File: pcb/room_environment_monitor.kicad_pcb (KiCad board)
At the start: 2 copper layers, 1 part, among them U2 ESP32-C3-MINI-1

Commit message: get the schematic done, need to optomize for parts
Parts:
- added U1: D1213A-04V, Package_TO_SOT_SMD:SOT-363_SC-70-6, F.Cu at (1.62, 1.43)
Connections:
- net Net-(U2-GND-Pad1) renamed GND
- U2 pad 22: unconnected-(U2-GPIO8-Pad22) -> I2C_SCL
- U2 pad 23: unconnected-(U2-GPIO9-Pad23) -> I2C_SDA
- U2 pad 26: unconnected-(U2-GPIO18/USB_D--Pad26) -> USB_D-
- U2 pad 27: unconnected-(U2-GPIO19/USB_D+-Pad27) -> USB_D+
- U2 pad 3: unconnected-(U2-3V3-Pad3) -> +3V3
- U2 pad 30: unconnected-(U2-GPIO20/U0RXD-Pad30) -> UART_RX
- U2 pad 31: unconnected-(U2-GPIO21/U0TXD-Pad31) -> UART_TX
- U2 pad 8: unconnected-(U2-EN/CHIP_PU-Pad8) -> EN

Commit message: WIP
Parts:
- added C1: 100n, Capacitor_SMD:C_0603_1608Metric, F.Cu at (-46.5, 31.6)
- added C10: 10u, Capacitor_SMD:C_0603_1608Metric, F.Cu at (-46.5, 39.1)
- added C11: 22u, Capacitor_SMD:C_0603_1608Metric, F.Cu at (-46.5, 41.6)
- added C12: 10u, Capacitor_SMD:C_0603_1608Metric, F.Cu at (-42.5, 31.6)
- added C13: 1u, Capacitor_SMD:C_0603_1608Metric, F.Cu at (-42.5, 34.1)
- added C14: 10u, Capacitor_SMD:C_0603_1608Metric, F.Cu at (-42.5, 36.6)
- added C2: 100n, Capacitor_SMD:C_0603_1608Metric, F.Cu at (-46.5, 34.1)
- added C3: 0.1u, Capacitor_SMD:C_0603_1608Metric, F.Cu at (-46.5, 36.6)
- added C4: 100n, Capacitor_SMD:C_0603_1608Metric, F.Cu at (-28.5, 41.5)
- added C5: 100n, Capacitor_SMD:C_0603_1608Metric, F.Cu at (-28.5, 44.1)
- added D1: MBR1020VL, Diode_SMD:D_SOD-123F, F.Cu at (-35.7, 57.9)
- added D2: LED, LED_SMD:LED_0603_1608Metric, F.Cu at (-34.6, 44.2)
- added D3: SK6812MINI, LED_SMD:LED_SK6812MINI_PLCC4_3.5x3.5mm_P1.75mm, F.Cu at (-45.0, 45.4)
- added D4: SK6812MINI, LED_SMD:LED_SK6812MINI_PLCC4_3.5x3.5mm_P1.75mm, F.Cu at (-45.0, 50.5)
- added D5: SK6812MINI, LED_SMD:LED_SK6812MINI_PLCC4_3.5x3.5mm_P1.75mm, F.Cu at (-45.0, 55.5)
- added D7: LED, LED_SMD:LED_0603_1608Metric, F.Cu at (-34.6, 46.8)
- added D8: LED, LED_SMD:LED_0603_1608Metric, F.Cu at (-34.6, 49.4)
- added J1: Conn_01x02_Pin, Connector_JST:JST_GH_BM02B-GHS-TBT_1x02-1MP_P1.25mm_Vertical, F.Cu at (-52.6, 52.3)
- added J2: Conn_01x04_Pin, Connector_JST:JST_ZE_BM04B-ZESS-TBT_1x04-1MP_P1.50mm_Vertical, F.Cu at (-23.7, 35.3)
- added P1: USB_C_Plug_USB2.0, Kevin_Lutzer_Lbr:CONN6_USB4130-GF-C_GCT, F.Cu at (110.0, 140.5)
- added Q3: BSS138, Package_TO_SOT_SMD:SOT-23, F.Cu at (-39.1, 45.1)
- added Q4: BSS138, Package_TO_SOT_SMD:SOT-23, F.Cu at (-24.0, 42.5)
- added Q5: BSS138, Package_TO_SOT_SMD:SOT-23, F.Cu at (-24.0, 47.0)
- added Q6: BSS138, Package_TO_SOT_SMD:SOT-23, F.Cu at (-39.1, 49.6)
- added Q7: BSS138, Package_TO_SOT_SMD:SOT-23, F.Cu at (-39.1, 54.0)
- added R1: 10k, Resistor_SMD:R_0603_1608Metric, F.Cu at (-42.5, 39.1)
- added R12: 10k, Resistor_SMD:R_0603_1608Metric, F.Cu at (-38.5, 31.6)
- added R13: NC, Resistor_SMD:R_0603_1608Metric, F.Cu at (-38.5, 34.1)
- added R14: 22.1k, Resistor_SMD:R_0603_1608Metric, F.Cu at (-38.5, 36.6)
- added R15: 47.5k, Resistor_SMD:R_0603_1608Metric, F.Cu at (-38.5, 39.1)
- added R16: 0, Resistor_SMD:R_0603_1608Metric, F.Cu at (-38.5, 41.6)
- added R17: 0, Resistor_SMD:R_0603_1608Metric, F.Cu at (-34.5, 31.6)
- added R18: 220, Resistor_SMD:R_0603_1608Metric, F.Cu at (-34.5, 34.1)
- added R19: 220, Resistor_SMD:R_0603_1608Metric, F.Cu at (-34.5, 36.6)
- added R2: 220, Resistor_SMD:R_0603_1608Metric, F.Cu at (-42.5, 41.6)
- added R20: 5.1k, Resistor_SMD:R_0603_1608Metric, F.Cu at (-34.5, 39.1)
- added R21: 10k, Resistor_SMD:R_0603_1608Metric, F.Cu at (-34.5, 41.6)
- added R3: 10k, Resistor_SMD:R_0603_1608Metric, F.Cu at (-28.5, 46.6)
- added R4: 10k, Resistor_SMD:R_0603_1608Metric, F.Cu at (-28.5, 49.1)
- added RN1: 10k, Resistor_SMD:R_Array_Concave_4x0603, F.Cu at (-19.5, 47.3)
- added SW1: SW_SPST, Button_Switch_SMD:SW_Push_1P1T_NO_CK_KMR2, F.Cu at (-59.9, 50.8)
- added SW2: SW_SPST, Button_Switch_SMD:SW_Push_1P1T_NO_CK_KMR2, F.Cu at (-59.9, 55.4)
- added TP1: TestPoint, TestPoint:TestPoint_Pad_D1.0mm, F.Cu at (-40.0, 57.8)
- added TP2: TestPoint, TestPoint:TestPoint_Pad_D1.0mm, F.Cu at (-15.4, 31.9)
- added TP3: TestPoint, TestPoint:TestPoint_Pad_D1.0mm, F.Cu at (-15.4, 34.9)
- added TP4: TestPoint, TestPoint:TestPoint_Pad_D1.0mm, F.Cu at (-40.0, 60.8)
- added U3: SGP30-2.5K, Kevin_Lutzer_Lbr:SGP30-2.5K_SEN-M, F.Cu at (-18.4, 42.6)
- added U4: BME280, Package_LGA:Bosch_LGA-8_2.5x2.5mm_P0.65mm_ClockwisePinNumbering, F.Cu at (-15.5, 47.0)
- added U7: AZ1117-3.3, Package_TO_SOT_SMD:SOT-23-5, F.Cu at (-60.7, 60.0)
- added U8: CP2102N-Axx-xQFN28, Package_DFN_QFN:QFN-28-1EP_5x5mm_P0.5mm_EP3.35x3.35mm, F.Cu at (-53.0, 59.7)
- moved U2 220.5 mm to (-55.9, 39.4)
- moved U1 75.7 mm to (-46.4, 60.0)
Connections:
- U2 pad 16: unconnected-(U2-GPIO10-Pad16) -> FAN
- U2 pad 18: unconnected-(U2-GPIO4/ADC1_CH4-Pad18) -> UART1_RX
- U2 pad 19: unconnected-(U2-GPIO5/ADC2_CH0-Pad19) -> UART1_TX
- U2 pad 20: unconnected-(U2-GPIO6-Pad20) -> I2C_SCL
- U2 pad 21: unconnected-(U2-GPIO7-Pad21) -> I2C_SDA
- U2 pad 22: I2C_SCL -> NEOPIXEL
- U2 pad 23: I2C_SDA -> BOOT
- U2 pad 26: USB_D- -> unconnected-(U2-GPIO18/USB_D--Pad26)
- U2 pad 27: USB_D+ -> unconnected-(U2-GPIO19/USB_D+-Pad27)
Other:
- board outline added: 20 x 73 mm

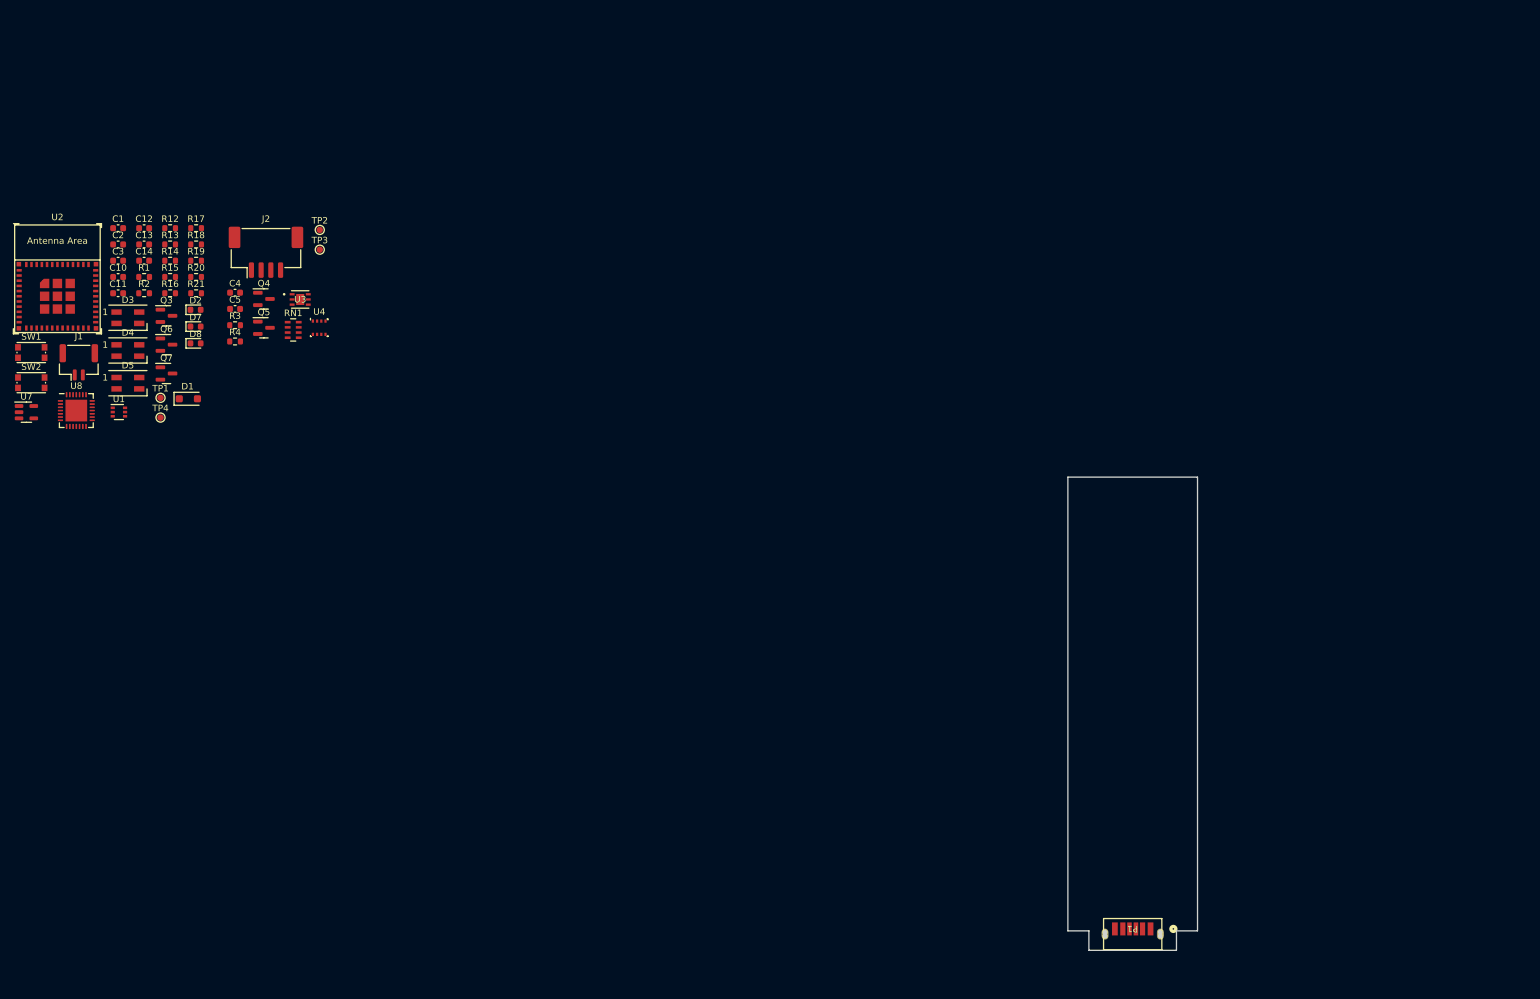
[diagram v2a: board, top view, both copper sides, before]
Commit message: finish the routing need to move the esp32 up 5.5 mm
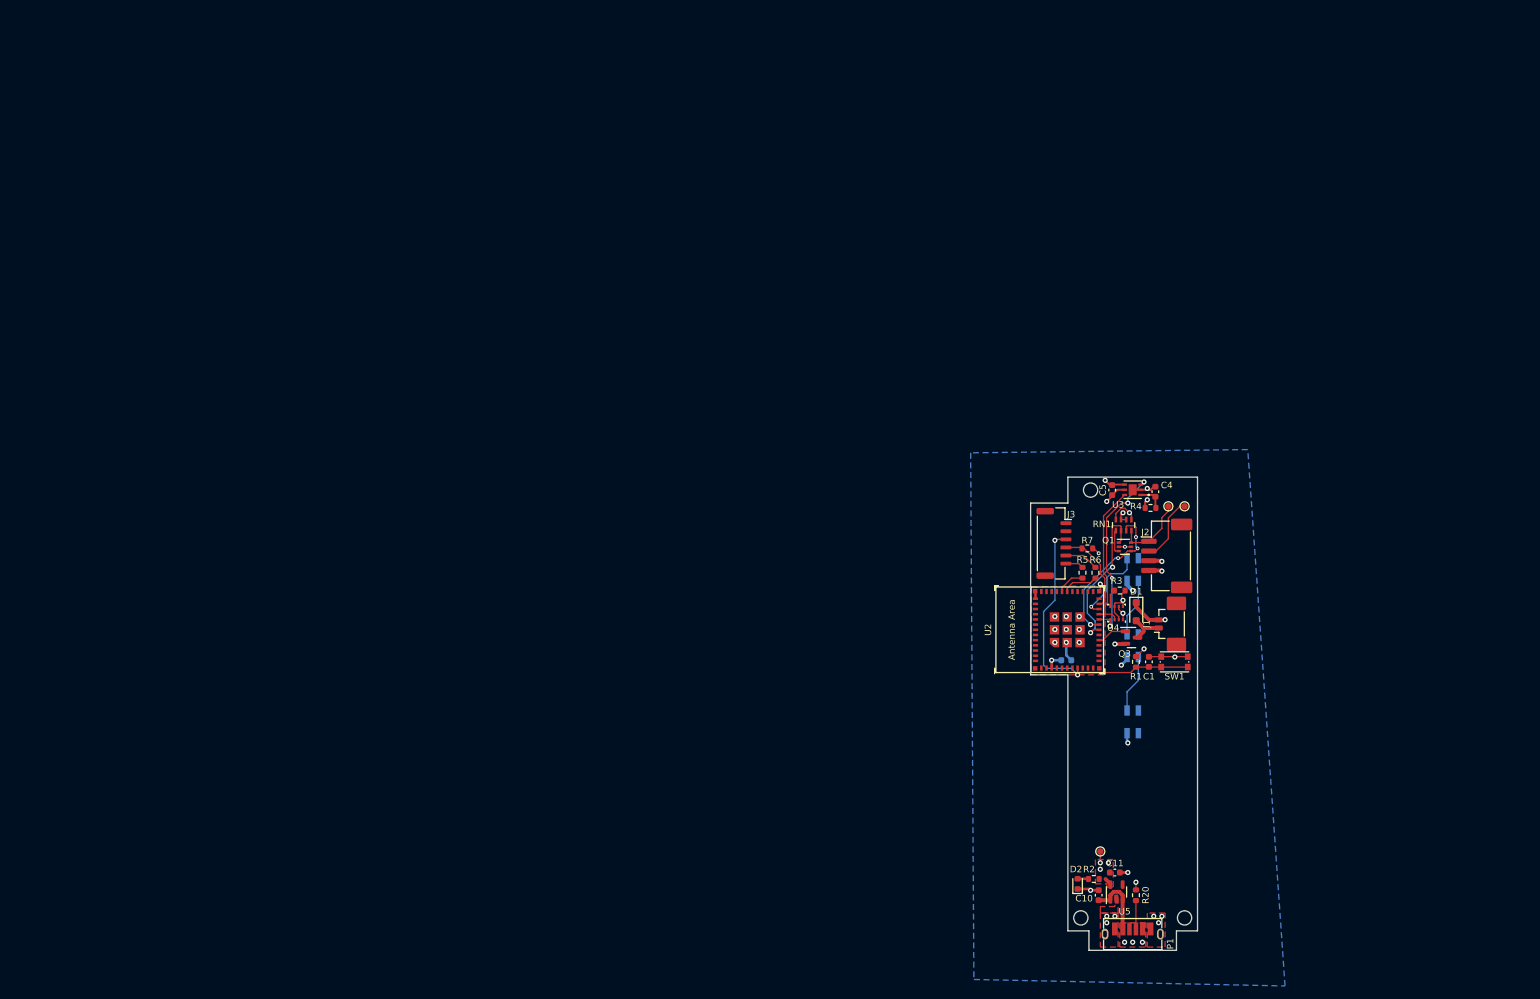
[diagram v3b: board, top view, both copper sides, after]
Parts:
- removed C12, C14: 10u, Capacitor_SMD:C_0603_1608Metric
- removed C13: 1u, Capacitor_SMD:C_0603_1608Metric
- removed C2: 100n, Capacitor_SMD:C_0603_1608Metric
- removed D7, D8: LED, LED_SMD:LED_0603_1608Metric
- removed Q4, Q5, Q6, Q7: BSS138, Package_TO_SOT_SMD:SOT-23
- removed R12, R21: 10k, Resistor_SMD:R_0603_1608Metric
- removed R13: NC, Resistor_SMD:R_0603_1608Metric
- removed R14: 22.1k, Resistor_SMD:R_0603_1608Metric
- removed R15: 47.5k, Resistor_SMD:R_0603_1608Metric
- removed R16, R17: 0, Resistor_SMD:R_0603_1608Metric
- removed R18, R19: 220, Resistor_SMD:R_0603_1608Metric
- removed SW2: SW_SPST, Button_Switch_SMD:SW_Push_1P1T_NO_CK_KMR2
- removed TP1: TestPoint, TestPoint:TestPoint_Pad_D1.0mm
- removed U1: D1213A-04V, Package_TO_SOT_SMD:SOT-363_SC-70-6
- removed U7: AZ1117-3.3, Package_TO_SOT_SMD:SOT-23-5
- removed U8: CP2102N-Axx-xQFN28, Package_DFN_QFN:QFN-28-1EP_5x5mm_P0.5mm_EP3.35x3.35mm
- added H1: MountingHole, MountingHole:MountingHole_2.2mm_M2_DIN965, F.Cu at (102.0, 138.0)
- added H2: MountingHole, MountingHole:MountingHole_2.2mm_M2_DIN965, F.Cu at (118.0, 138.0)
- added H3: MountingHole, MountingHole:MountingHole_2.2mm_M2_DIN965, F.Cu at (103.5, 72.0)
- added J3: Conn_01x06_Socket, Connector_JST:JST_GH_SM06B-GHS-TB_1x06-1MP_P1.25mm_Horizontal, F.Cu at (97.8, 80.2)
- added Q1: Q_Dual_NMOS_G1S2G2D2S1D1, Package_TO_SOT_SMD:SOT-363_SC-70-6, F.Cu at (108.8, 80.8)
- added R5: 0, Resistor_SMD:R_0603_1608Metric, F.Cu at (102.2, 84.8)
- added R6: 0, Resistor_SMD:R_0603_1608Metric, F.Cu at (104.2, 84.8)
- added R7: 10k, Resistor_SMD:R_0603_1608Metric, F.Cu at (103.0, 81.0)
- added U5: AP2112K-3.3, Package_TO_SOT_SMD:SOT-23-5, F.Cu at (107.5, 134.0)
- C3, D3, D4, D5: moved to B.Cu
- J1: footprint Connector_JST:JST_GH_BM02B-GHS-TBT_1x02-1MP_P1.25mm_Vertical -> Connector_Molex:Molex_PicoBlade_53398-0271_1x02-1MP_P1.25mm_Vertical
- moved SW1 182.7 mm to (116.5, 98.5)
- moved C10 178.8 mm to (104.8, 134.5), turned to 90 degrees
- moved C11 177.9 mm to (107.2, 131.0)
- moved R20 173.6 mm to (110.5, 134.5), turned to 90 degrees
- moved J1 172.6 mm to (115.2, 92.7), turned to 90 degrees
- moved C1 172.5 mm to (112.5, 98.5), turned to 90 degrees
- moved R2 172.1 mm to (104.0, 132.0), turned to 180 degrees
- moved R1 164.1 mm to (110.5, 98.5), turned to -90 degrees
- moved D5 163.6 mm to (110.0, 107.8), turned to 90 degrees
- moved U2 162.4 mm to (97.2, 93.5), turned to 90 degrees
- moved D2 162.4 mm to (101.5, 132.8), turned to 90 degrees
- moved D4 161.6 mm to (110.0, 96.0), turned to 90 degrees
- moved D3 159.8 mm to (110.0, 84.2), turned to 90 degrees
- moved TP4 159.7 mm to (105.0, 127.8)
- moved C3 158.7 mm to (99.8, 98.2)
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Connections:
- C10 pad 2: Net-(C10-Pad2) -> GND
- C11 pad 2: Net-(C10-Pad2) -> GND
- D3 pad 4: +3V3 -> +5V
- D4 pad 4: +3V3 -> +5V
- D5 pad 4: +3V3 -> +5V
- RN1 pad 1: UART1_RX -> UART1_TX
- RN1 pad 2: UART1_TX -> UART1_RX_LVL
- RN1 pad 3: UART1_RX_LVL -> UART1_TX_LVL
- RN1 pad 4: UART1_TX_LVL -> UART1_RX
- RN1 pad 5: +3V3 -> +5V
- RN1 pad 7: +5V -> +3V3
- U2 pad 18: UART1_RX -> UART1_RX_LVL
- U2 pad 19: UART1_TX -> UART1_TX_LVL
- U3 pad 3: I2C_SDA_LVL -> I2C_SCL
- U3 pad 6: I2C_SCL_LVL -> I2C_SDA
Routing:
- net EN: track 0.00 -> 45.6 mm, vias 0 -> 2
- net GND: track 0.00 -> 35.2 mm, vias 0 -> 28
- net I2C_SCL: track 0.00 -> 29.2 mm, vias 0 -> 4
- net +5V: track 0.00 -> 24.8 mm, vias 0 -> 7
- net UART1_RX_LVL: track 0.00 -> 24.7 mm, vias 0 -> 2
- net UART1_TX_LVL: track 0.00 -> 23.7 mm, vias 0 -> 4
- net I2C_SDA: track 0.00 -> 23.2 mm
- net +3V3: track 0.00 -> 22.1 mm, vias 0 -> 10
- net UART1_TX: track 0.00 -> 14.0 mm
- net BOOT: track 0.00 -> 13.3 mm
- net NEOPIXEL: track 0.00 -> 12.2 mm, vias 0 -> 1
- net UART1_RX: track 0.00 -> 11.3 mm
- net Net-(D4-DOUT): track 0.00 -> 8.97 mm
- net Net-(D3-DOUT): track 0.00 -> 8.97 mm
- net UART_RX: track 0.00 -> 5.53 mm
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- added copper zone on F.Cu, net +3V3
- added copper zone on In2.Cu, net +3V3
- added copper zone on B.Cu, net +5V
- added copper zone on F.Cu, net +5V
- added copper zone on F.Cu, net GND
- added copper zone on In1.Cu, net GND
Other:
- board size 20 x 73 mm -> 25.8 x 73 mm
- copper layers 2 -> 4

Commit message: finish routing the PCB
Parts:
- removed SW1: SW_SPST, Button_Switch_SMD:SW_Push_1P1T_NO_CK_KMR2
- C3: moved to F.Cu
- J3: footprint Connector_JST:JST_GH_SM06B-GHS-TB_1x06-1MP_P1.25mm_Horizontal -> Connector_JST:JST_SH_SM06B-SRSS-TB_1x06-1MP_P1.00mm_Horizontal; moved to B.Cu
- U3: footprint Kevin_Lutzer_Lbr:SGP30-2.5K_SEN-M -> Kevin_Lutzer_Lbr:SGP30-2.5K_SEN-L
- moved C4 15.2 mm to (110.0, 87.0), turned to -90 degrees
- moved U3 14.0 mm to (107.6, 85.8), turned to -90 degrees
- moved R1 11.4 mm to (100.6, 92.8), turned to 0 degrees
- moved C5 11.0 mm to (107.6, 83.0), turned to 0 degrees
- moved C1 10.3 mm to (104.0, 92.8), turned to 0 degrees
- moved R4 9.46 mm to (110.0, 83.8), turned to -90 degrees
- moved R5 9.04 mm to (97.6, 77.0), turned to 180 degrees
- moved U2 8.65 mm to (97.4, 84.9)
- moved R6 8.40 mm to (101.0, 77.0), turned to 0 degrees
- moved C3 6.15 mm to (97.0, 92.8), turned to 180 degrees
- moved J3 4.68 mm to (97.8, 84.9), turned to 90 degrees
- moved R7 4.24 mm to (104.4, 77.0), turned to 0 degrees
- moved R3 4.22 mm to (110.2, 91.1), turned to -90 degrees
- moved Q3 1.88 mm to (111.7, 94.6)
- moved D1 1.87 mm to (112.4, 90.5)
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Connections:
- J1 pad 1: +5V -> Net-(D1-A)
- J1 pad 2: Net-(D1-A) -> +5V
- J3 pad 1: unconnected-(J3-Pin_1-Pad1) -> +5V
- J3 pad 2: unconnected-(J3-Pin_2-Pad2) -> GND
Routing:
- net EN: track 45.6 -> 9.90 mm, vias 2 -> 1
- net I2C_SCL: track 29.2 -> 9.62 mm, vias 4 -> 0
- net UART1_RX_LVL: track 24.7 -> 15.0 mm
- net FAN: track 4.63 -> 13.8 mm, vias 0 -> 2
- net NEOPIXEL: track 12.2 -> 19.7 mm
- net UART1_TX_LVL: track 23.7 -> 17.2 mm, vias 4 -> 3
- net UART1_TX: track 14.0 -> 19.8 mm
- net I2C_SDA: track 23.2 -> 17.9 mm, vias 0 -> 2
- net Net-(J3-Pin_5): track 5.31 -> 9.88 mm, vias 0 -> 1
- net Net-(D3-DOUT): track 8.97 -> 12.9 mm
- net Net-(J3-Pin_6): track 2.79 -> 6.66 mm, vias 0 -> 1
- net UART_RX: track 5.53 -> 1.92 mm
- net GND: track 35.2 -> 31.9 mm, vias 28 -> 22
- net +3V3: track 22.1 -> 24.9 mm, vias 10 -> 11
- net UART_TX: track 4.36 -> 2.36 mm
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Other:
- board size 25.8 x 73 mm -> 25.5 x 73 mm

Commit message: finish v4 and the images for doucmentation
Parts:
- removed RN1: 10k, Resistor_SMD:R_Array_Concave_4x0603
- added C2: 0u1, Capacitor_SMD:C_0603_1608Metric, F.Cu at (110.0, 89.2)
- added D6: D_Photo, Diode_SMD:D_1206_3216Metric_Pad1.42x1.75mm_HandSolder, B.Cu at (110.0, 75.8)
- added R10: 2k2, Resistor_SMD:R_0603_1608Metric, F.Cu at (109.0, 81.2)
- added R11: 2k2, Resistor_SMD:R_0603_1608Metric, F.Cu at (109.0, 83.0)
- added R12: 10k, Resistor_SMD:R_0603_1608Metric, F.Cu at (108.8, 73.2)
- added R13: 10k, Resistor_SMD:R_0603_1608Metric, F.Cu at (110.5, 73.2)
- added R14: R_Small_US, Resistor_SMD:R_0603_1608Metric, F.Cu at (107.0, 73.3)
- added R8: 0, Resistor_SMD:R_0603_1608Metric, F.Cu at (109.0, 79.5)
- added R9: 0, Resistor_SMD:R_0603_1608Metric, F.Cu at (112.2, 73.2)
- added REF**: KiCad-Logo2_5mm_SilkScreen, Symbol:KiCad-Logo2_5mm_SilkScreen, F.Cu at (113.4, 117.0)
- added REF**: OSHW-Logo2_7.3x6mm_SilkScreen, Symbol:OSHW-Logo2_7.3x6mm_SilkScreen, F.Cu at (103.8, 118.8)
- added SW1: SW_SPST, Button_Switch_SMD:SW_Push_1P1T_NO_CK_KMR2, F.Cu at (100.7, 93.8)
- added TP1: TestPoint, TestPoint:TestPoint_Pad_D1.0mm, F.Cu at (120.0, 90.0)
- added kibuzzard-652F08CD: G***, kibuzzard-652F08CD, F.Cu at (116.4, 72.4)
- added kibuzzard-652F0EDE: G***, kibuzzard-652F0EDE, F.Cu at (105.1, 126.1)
- added kibuzzard-652F0FC5: G***, kibuzzard-652F0FC5, F.Cu at (118.0, 88.5)
- added kibuzzard-652F2D51: G***, kibuzzard-652F2D51, F.Cu at (100.8, 96.5)
- added kibuzzard-652F50CA: G***, kibuzzard-652F50CA, F.Cu at (110.0, 112.8)
- added kibuzzard-652F5449: G***, kibuzzard-652F5449, F.Cu at (102.7, 114.6)
- C1, C4, C5: value 100n -> 0u1
- C3: value 0.1u -> 0u1
- D1: value MBR1020VL -> CDBMS160
- Q1: value Q_Dual_NMOS_G1S2G2D2S1D1 -> BSS138; footprint Package_TO_SOT_SMD:SOT-363_SC-70-6 -> Package_TO_SOT_SMD:SOT-23
- U3: footprint Kevin_Lutzer_Lbr:SGP30-2.5K_SEN-L -> Kevin_Lutzer_Lbr:SGP30-2.5K_SEN
- moved C5 13.4 mm to (114.5, 94.5), turned to 180 degrees
- moved R4 11.7 mm to (109.5, 95.5), turned to 90 degrees
- moved D1 9.97 mm to (122.3, 89.2)
- moved J1 9.97 mm to (126.1, 91.5)
- moved Q3 9.97 mm to (121.6, 93.2)
- moved C4 8.79 mm to (107.8, 95.5)
- moved U4 6.86 mm to (114.5, 92.1), turned to 90 degrees
- moved R3 6.81 mm to (117.0, 92.0), turned to 90 degrees
- moved U3 6.56 mm to (109.6, 92.1), turned to 90 degrees
- moved R1 5.06 mm to (105.2, 94.8), turned to 180 degrees
- moved Q1 4.01 mm to (108.6, 76.8)
- moved TP3 2.85 mm to (115.2, 74.3)
- moved TP2 2.17 mm to (117.6, 74.3)
- moved H1 1.70 mm to (102.5, 139.2)
- moved H2 1.70 mm to (117.5, 139.2)
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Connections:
- J2 pad 1: UART1_RX -> Net-(J2-Pin_1)
- J2 pad 2: UART1_TX -> Net-(J2-Pin_2)
- Q1 pad 1: UART1_RX_LVL -> +3V3
- Q1 pad 2: +5V -> UART1_TX_LVL
- TP2 pad 1: UART1_RX -> Net-(J2-Pin_1)
- TP3 pad 1: UART1_TX -> Net-(J2-Pin_2)
- U2 pad 18: UART1_RX_LVL -> UART1_RX
- U2 pad 6: unconnected-(U2-GPIO3/ADC1_CH3-Pad6) -> PD
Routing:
- net PD: track 0.00 -> 36.4 mm, vias 0 -> 2
- net UART1_TX: track 19.8 -> 4.84 mm
- net UART1_RX_LVL: track 15.0 -> 0.00 mm, vias 2 -> 0
- net Net-(J2-Pin_2): track 0.00 -> 11.1 mm
- net Net-(J2-Pin_1): track 0.00 -> 10.4 mm, vias 0 -> 2
- net I2C_SCL: track 9.62 -> 17.6 mm
- net I2C_SDA: track 17.9 -> 24.7 mm
- net FAN: track 13.8 -> 20.2 mm
- net EN: track 9.90 -> 15.6 mm
- net +5V: track 23.2 -> 17.9 mm, vias 8 -> 7
- net GND: track 31.9 -> 37.1 mm, vias 22 -> 26
- net UART1_TX_LVL: track 17.2 -> 12.0 mm, vias 3 -> 2
- net UART1_RX: track 12.0 -> 7.22 mm, vias 0 -> 2
- net /Sensors/SGP30_VDD: track 4.79 -> 3.15 mm
- net +3V3: track 24.9 -> 26.3 mm, vias 11 -> 14
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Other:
- board size 25.5 x 73 mm -> 35.5 x 74.7 mm
